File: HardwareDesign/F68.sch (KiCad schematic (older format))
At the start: 0 parts

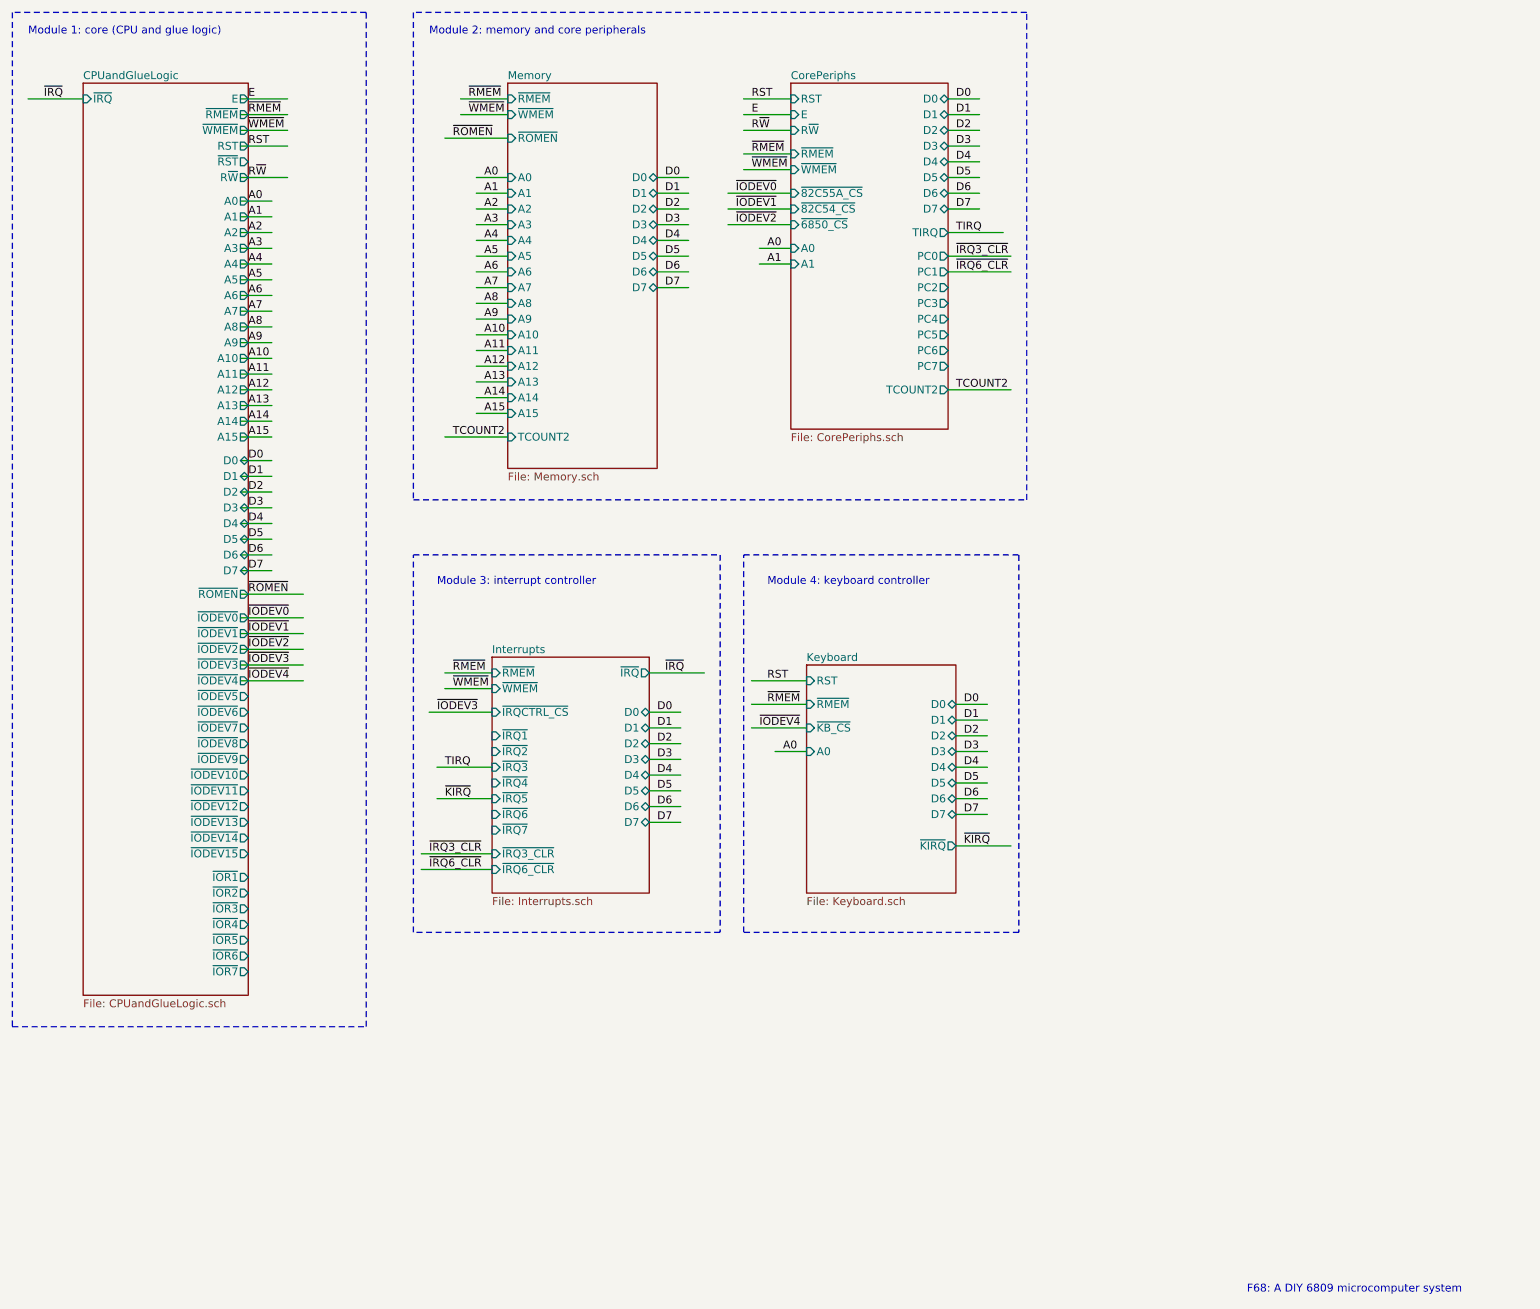
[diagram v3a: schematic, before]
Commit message: have one copy of backplane connector on main sheet
Avoids need to replicate it elsewhere, and helps ensure
that all signals are connected correctly.
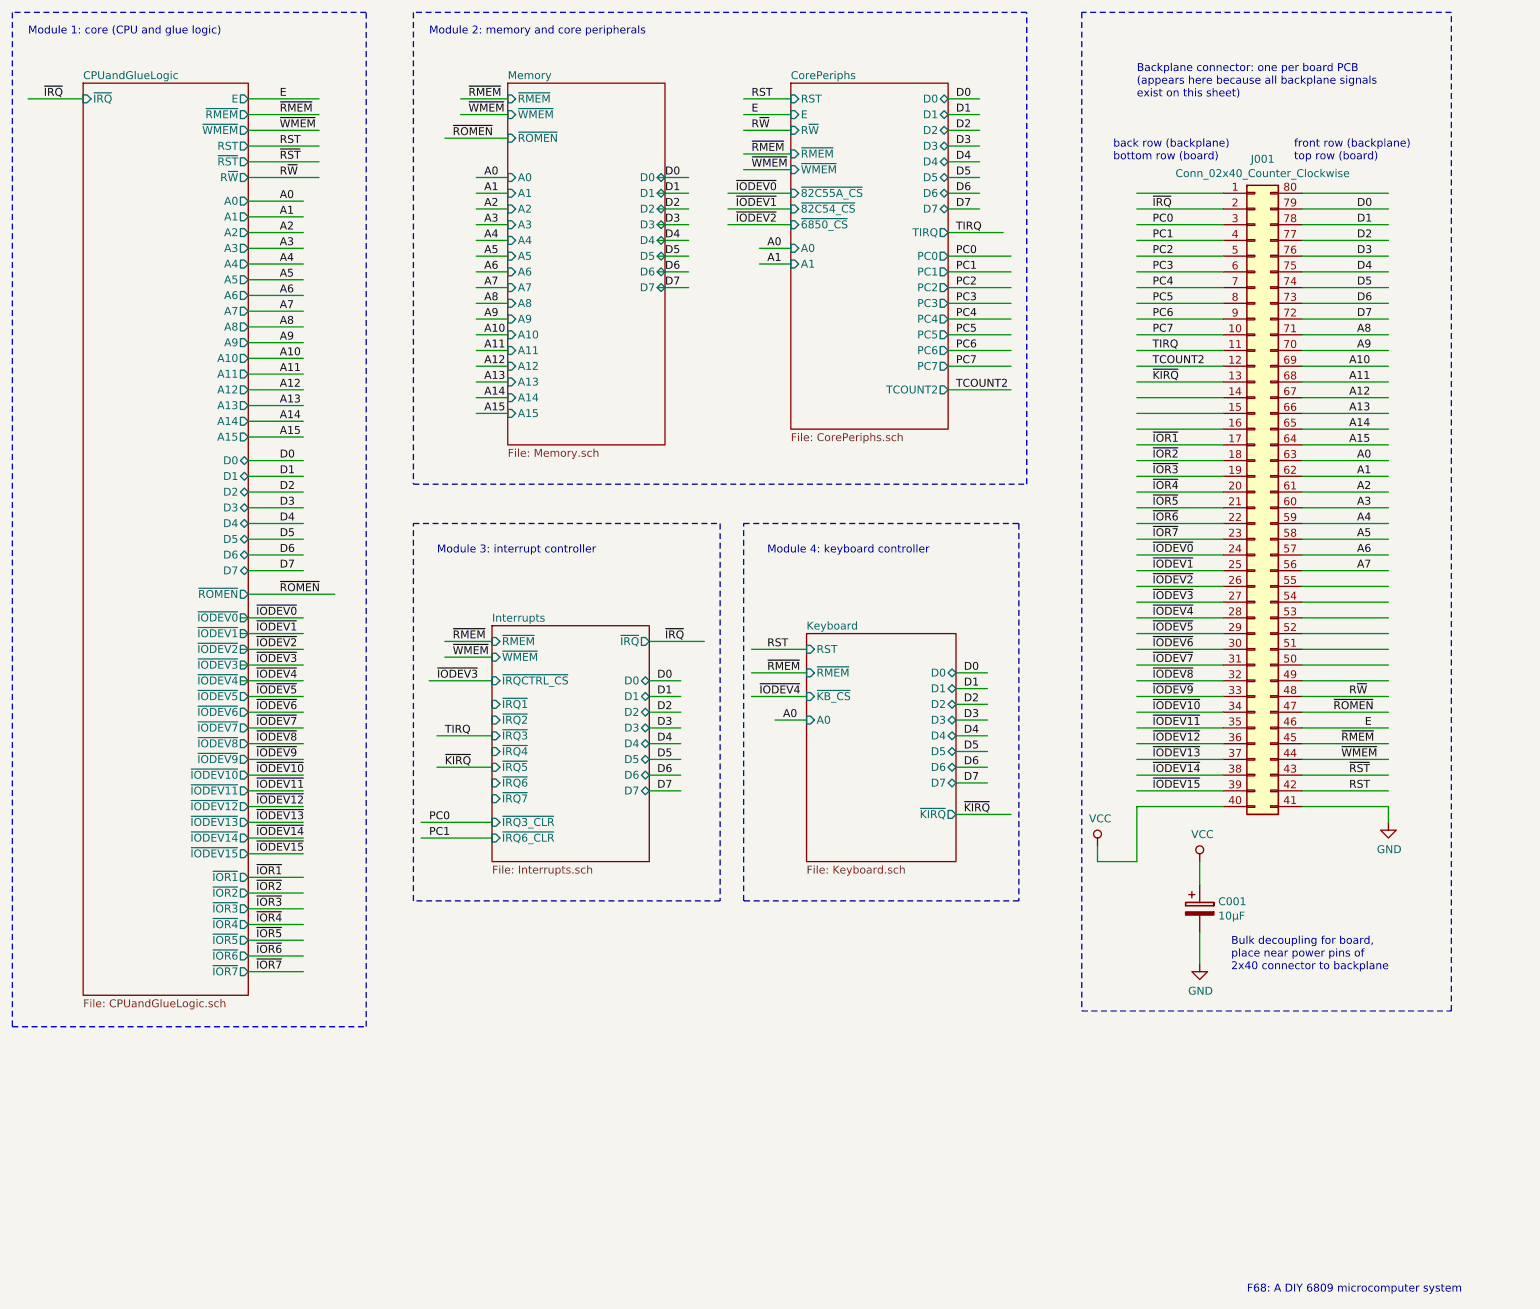
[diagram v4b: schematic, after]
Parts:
- added C001: 10μF, symbol device:CP
- added J001: Conn_02x40_Counter_Clockwise, symbol Connector_Generic:Conn_02x40_Counter_Clockwise
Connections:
- net labels added: GND, PC0, PC1, PC2, PC3, PC4, PC5, PC6, PC7, R~W~, VCC, ~IODEV10, ~IODEV11, ~IODEV12, ~IODEV13, ~IODEV14, ~IODEV15, ~IODEV5, ~IODEV6, ~IODEV7, ~IODEV8, ~IODEV9, ~IOR1~, ~IOR2~, ~IOR3~, ~IOR4~, ~IOR5~, ~IOR6~, ~IOR7~, ~RST~
- net labels removed: ~IRQ3_CLR, ~IRQ6_CLR
- wire segments 115 -> 225
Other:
- note added: "Backplane connector: one per board PCB\n(appears here because all backplane signals\nexist on this sheet)"
- note added: "Bulk decoupling for board,\nplace near power pins of\n2x40 connector to backplane"
- note added: "back row (backplane)\nbottom row (board)"
- note added: "front row (backplane)\ntop row (board)"

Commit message: fix R/-W signal on main sheet
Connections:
- net labels removed: R~W
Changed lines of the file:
@@
 	6700 2000 6400 2000
 Text Label 6450 2000 0    50   ~ 0
-R~W
+R~W~
 Wire Wire Line
 	3200 5300 3600 5300
